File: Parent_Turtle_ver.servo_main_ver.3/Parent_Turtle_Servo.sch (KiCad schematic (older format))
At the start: 54 parts, among them P1 CONN_02X15, P10 WRITING, P11 A/D, P12 5V_in, P13 CONN_02X04, P14 I/O, P15 CONN_02X04, P2 CONN_02X15, P3 CAN, P4 CAN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

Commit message: Increase pwm-pins
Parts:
- removed P5: PWM, Pin_Headers:Pin_Header_Straight_1x12, symbol CONN_01X12
- added D12: DIODE, Mizz_lib:SOD-123, symbol DIODE
- added P16: PWM, Pin_Headers:Pin_Header_Straight_1x02, symbol CONN_01X02
- added P5: PWM, Pin_Headers:Pin_Header_Straight_1x14, symbol CONN_01X14
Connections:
- net +3.3V: now also D12.2 (K)
- net A0: now also P5.4 (P4)
- net A1: now also P5.3 (P3)
- net A2: now also P5.6 (P6)
- net A3: now also P5.5 (P5)
- net A6: now also P5.8 (P8)
- net A7: now also P5.7 (P7)
- net B0: now also P5.10 (P10)
- net B1: now also P5.9 (P9)
- net B8: now also P16.1 (P1)
- net C9: now also P16.2 (P2)
- net E11: now also P5.12 (P12)
- net E13: now also P5.13 (P13)
- net E14: now also P5.14 (P14)
- net E5: now also P5.2 (P2)
- net E6: now also P5.1 (P1)
- net E9: now also P5.11 (P11)
- net at R9.1, SP1.2: now also D12.1 (A)
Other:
- moved on the sheet: Q1, R8, R9

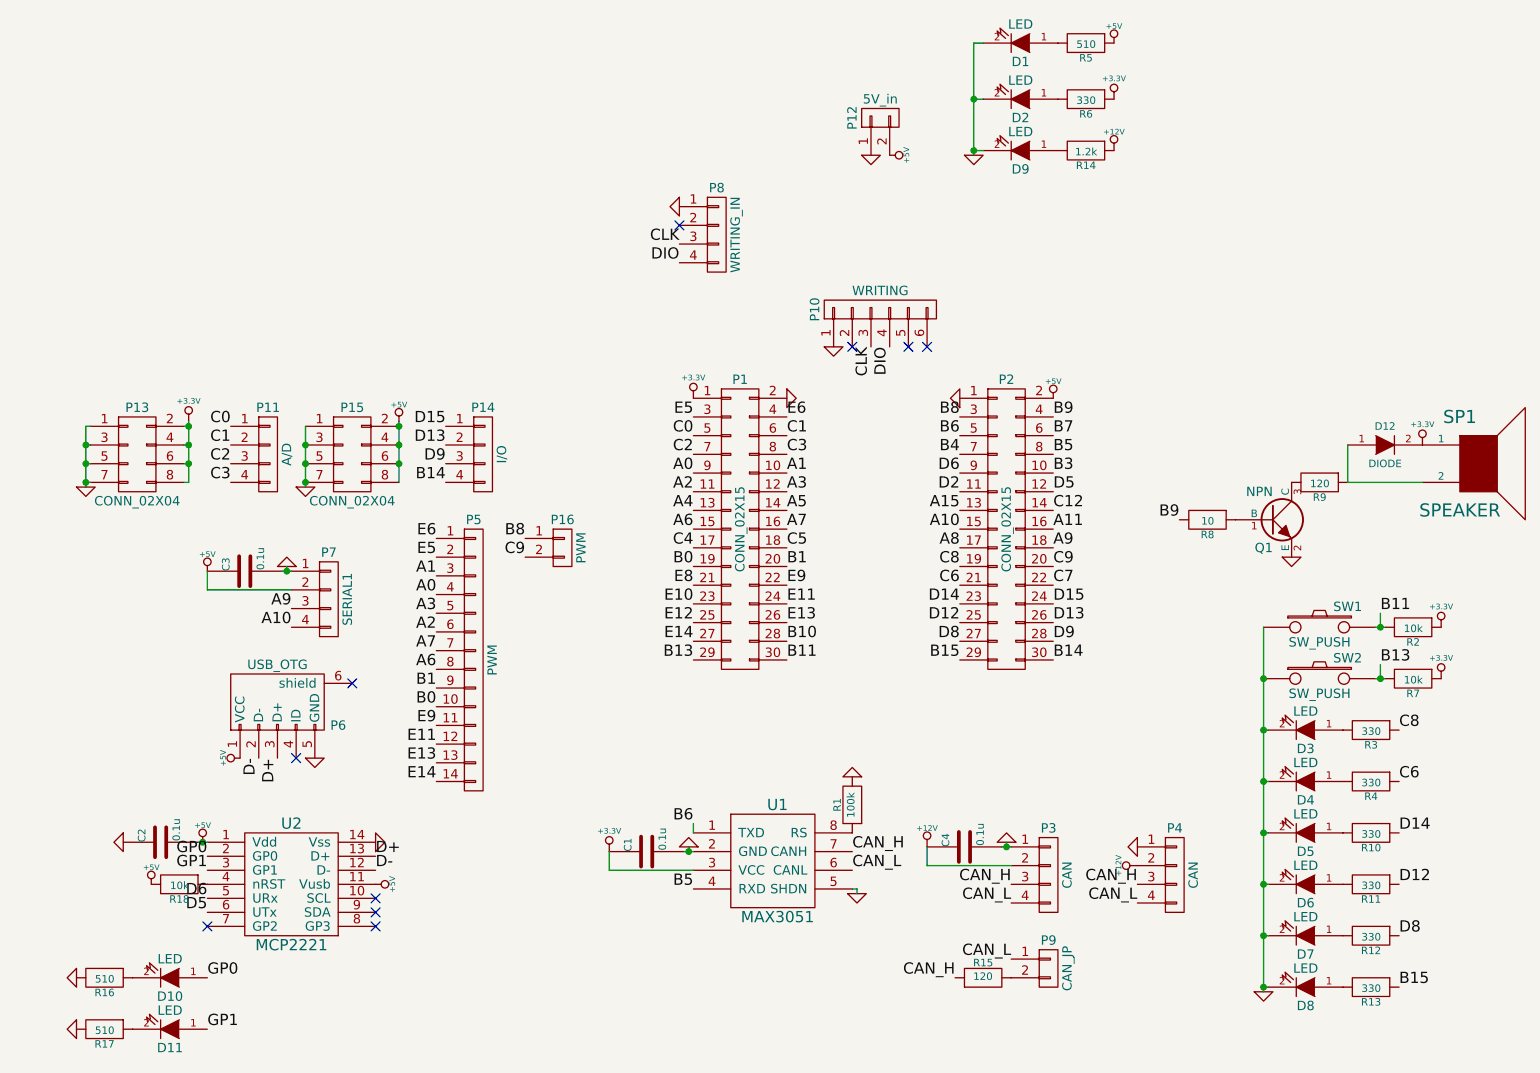
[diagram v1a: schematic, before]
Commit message: シリアル2まで追加
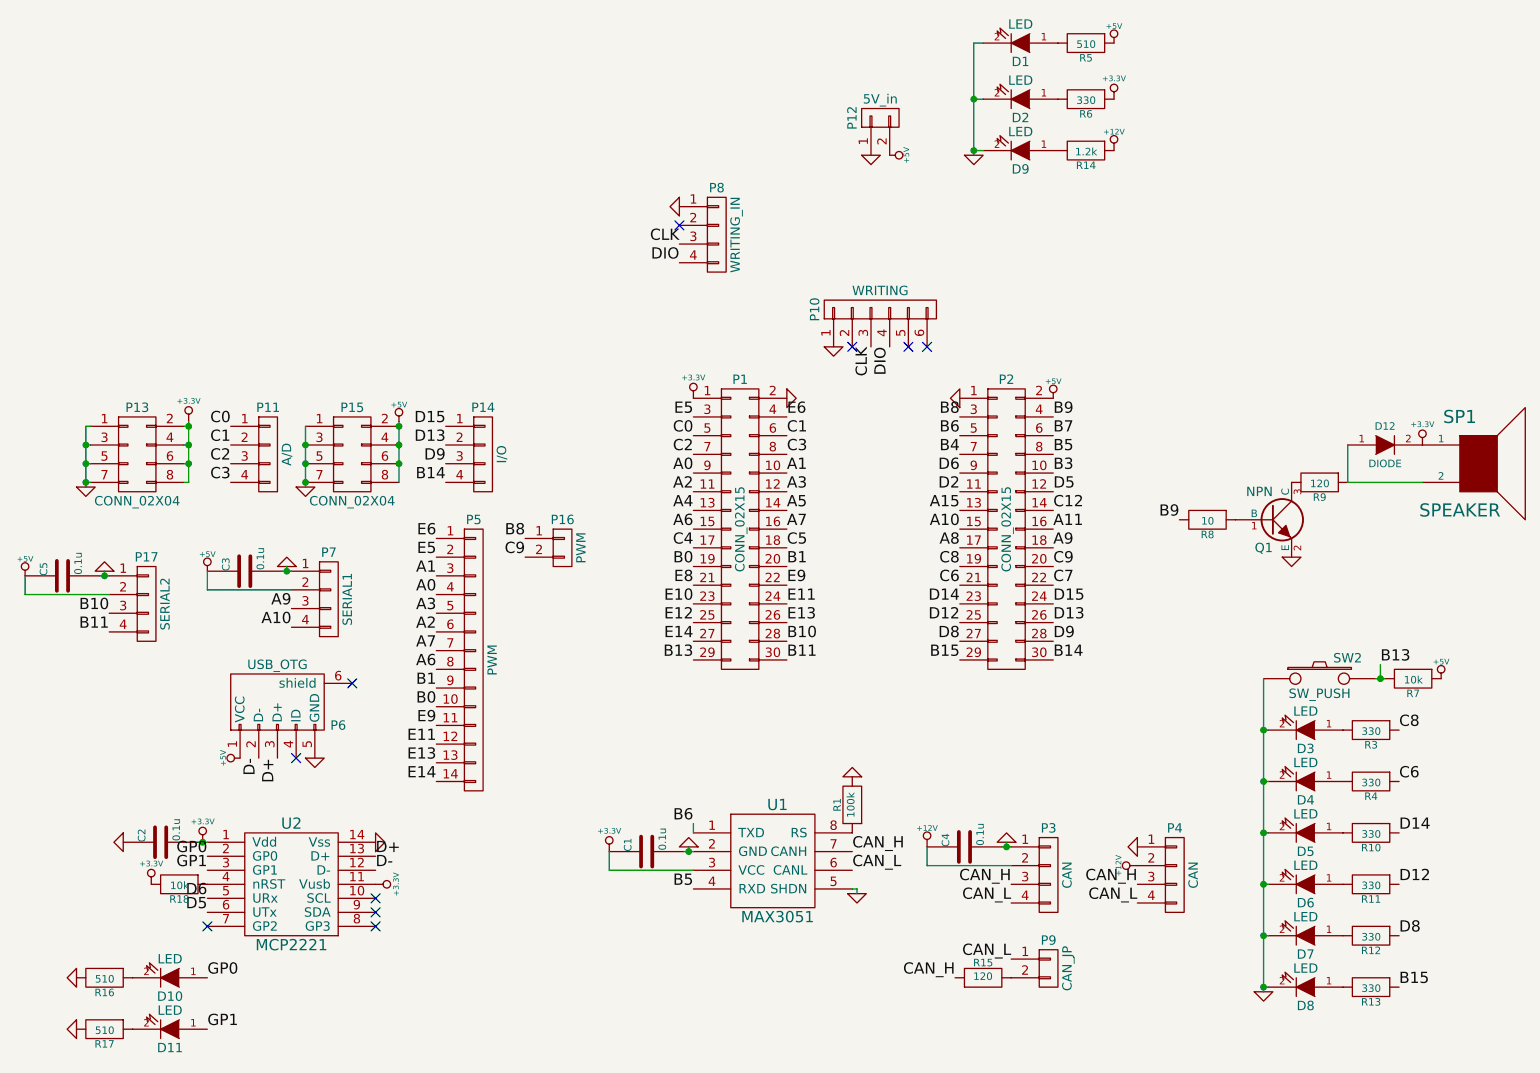
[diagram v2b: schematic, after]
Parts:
- removed R2: 10k, Resistors_SMD:R_0603, symbol R
- removed SW1: SW_PUSH, Buttons_Switches_ThroughHole:SW_PUSH_6mm, symbol SW_PUSH
- added C5: 0.1u, Capacitors_SMD:C_0603, symbol C
- added P17: SERIAL2, RP_KiCAD_Connector:XA_4T, symbol CONN_01X04
- SW2: footprint Buttons_Switches_ThroughHole:SW_PUSH_6mm -> Mizz_lib:RP_TroughHole_Button
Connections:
- net +3.3V: now also C2.2, R18.2, U2.1 (Vdd), U2.11 (Vusb); no longer R7.1
- net +5V: now also R7.1, C5.1, P17.2 (P2); no longer C2.2, R18.2, U2.1 (Vdd), U2.11 (Vusb)
- net B10: now also P17.3 (P3)
- net B11: now also P17.4 (P4)
- net GND: now also C5.2, P17.1 (P1)

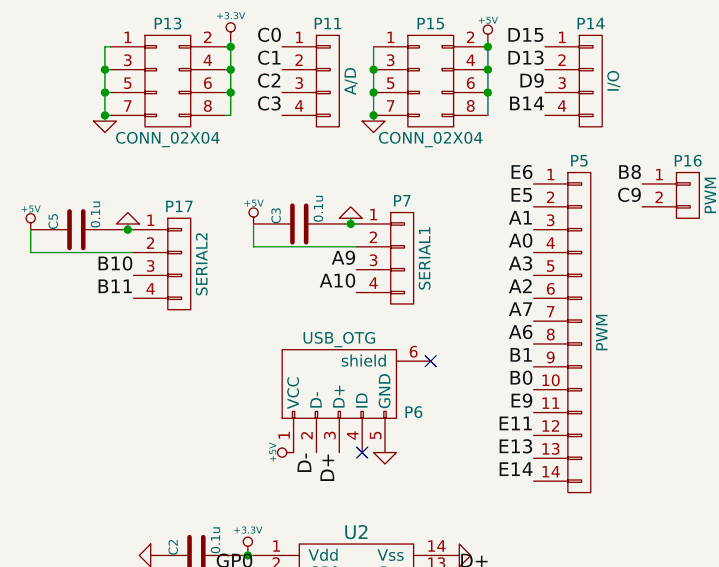
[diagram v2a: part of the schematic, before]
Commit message: シリアルの番号の整理
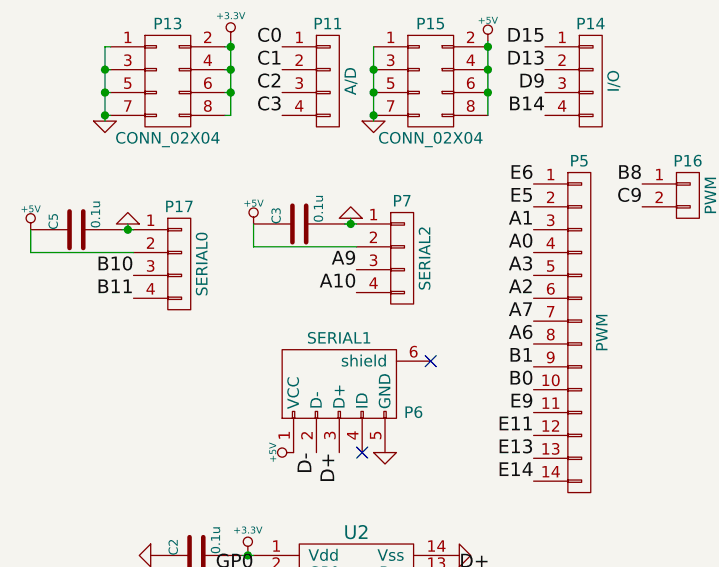
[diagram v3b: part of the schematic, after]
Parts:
- P17: value SERIAL2 -> SERIAL0
- P6: value USB_OTG -> SERIAL1
- P7: value SERIAL1 -> SERIAL2
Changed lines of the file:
@@
 P 3200 4225
 F 0 "P7" H 3200 4475 50  0000 C CNN
-F 1 "SERIAL1" V 3300 4225 50  0000 C CNN
+F 1 "SERIAL2" V 3300 4225 50  0000 C CNN
 F 2 "RP_KiCAD_Connector:XA_4T" H 3200 4225 50  0001 C CNN
 F 3 "" H 3200 4225 50  0000 C CNN
@@
 P 2925 4775
 F 0 "P6" H 3250 4650 50  0000 C CNN
-F 1 "USB_OTG" H 2925 4975 50  0000 C CNN
+F 1 "SERIAL1" H 2925 4975 50  0000 C CNN
 F 2 "Connect:USB_Mini-B" V 2875 4675 50  0001 C CNN
 F 3 "" V 2875 4675 50  0000 C CNN
@@
 P 2225 4250
 F 0 "P17" H 2225 4500 50  0000 C CNN
-F 1 "SERIAL2" V 2325 4250 50  0000 C CNN
+F 1 "SERIAL0" V 2325 4250 50  0000 C CNN
 F 2 "RP_KiCAD_Connector:XA_4T" H 2225 4250 50  0001 C CNN
 F 3 "" H 2225 4250 50  0000 C CNN

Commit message: main基板最終版
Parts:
- added C6, C7: 0.1u, Capacitors_SMD:C_0603, symbol C
- added R2: 10k, Resistors_SMD:R_0603, symbol R
- added SW1: SW1, Mizz_lib:RP_TroughHole_Button, symbol SW_PUSH
- added U3: 78L05, TO_SOT_Packages_SMD:SOT89-3_Housing, symbol 78L05
- D10, D11: footprint LEDs:LED-3MM -> LEDs:LED_0603
- SW2: value SW_PUSH -> SW0
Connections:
- net +12V: now also C6.1, U3.1 (VI)
- net +5V: now also C7.1, R2.1, U3.3 (VO)
- net B13: no longer R7.2, SW2.2
- net E10: now also R7.2, SW2.2
- net E12: now also R2.2, SW1.2
- net GND: now also C6.2, C7.2, SW1.1, U3.2 (GND)
